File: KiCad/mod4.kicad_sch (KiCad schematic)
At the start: 46 parts, among them M7 Fan_4pin, M8 Fan_4pin

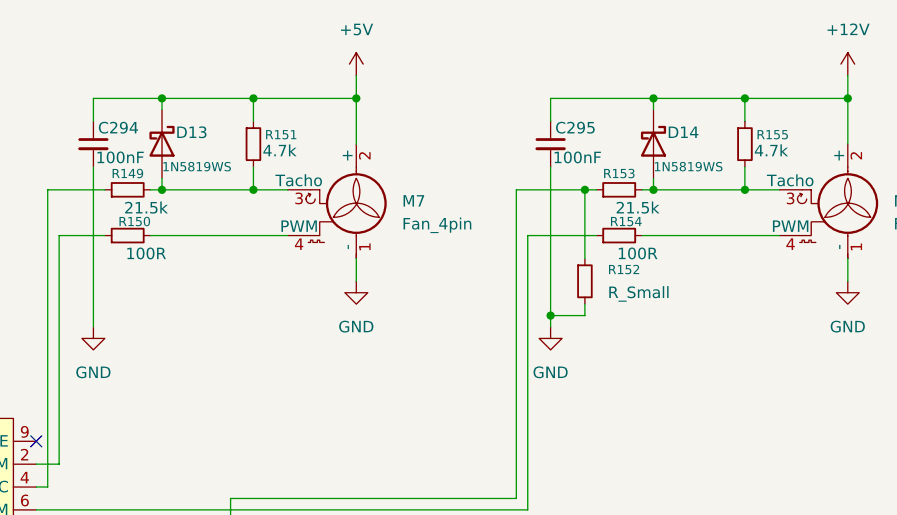
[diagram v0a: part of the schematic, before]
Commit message: Fix some diodes and resistors
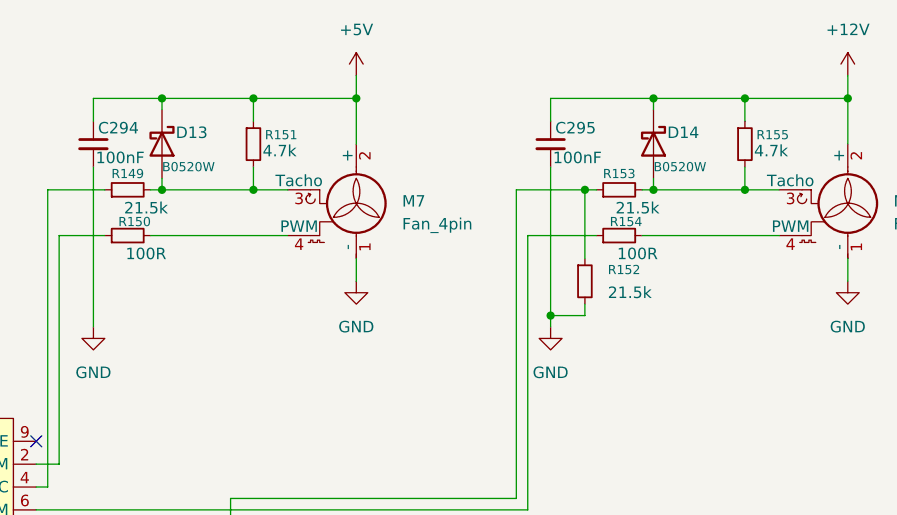
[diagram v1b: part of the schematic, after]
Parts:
- D13, D14: value 1N5819WS -> B0520W
- R152: value R_Small -> 21.5k
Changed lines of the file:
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@@
 			)
 		)
-		(property "Value" "R_Small"
+		(property "Value" "21.5k"
 			(at 391.16 68.5799 0)
 			(effects
@@
 			)
 		)
-		(property "Value" "1N5819WS"
+		(property "Value" "B0520W"
 			(at 396.24 54.61 90)
 			(effects
@@
 			)
 		)
-		(property "Value" "1N5819WS"
+		(property "Value" "B0520W"
 			(at 341.63 54.61 90)
 			(effects

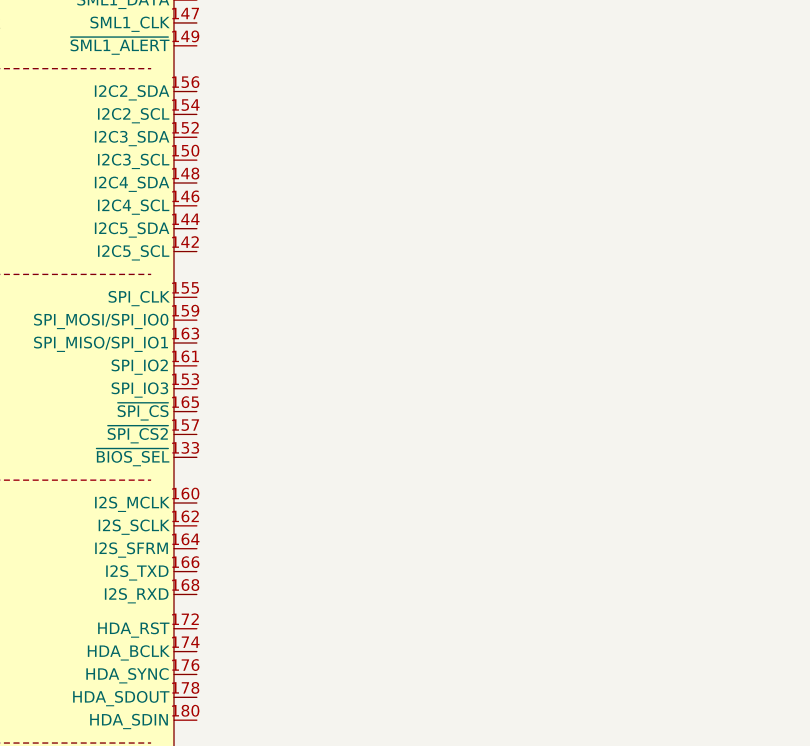
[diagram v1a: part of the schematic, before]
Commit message: Add external BIOS flash
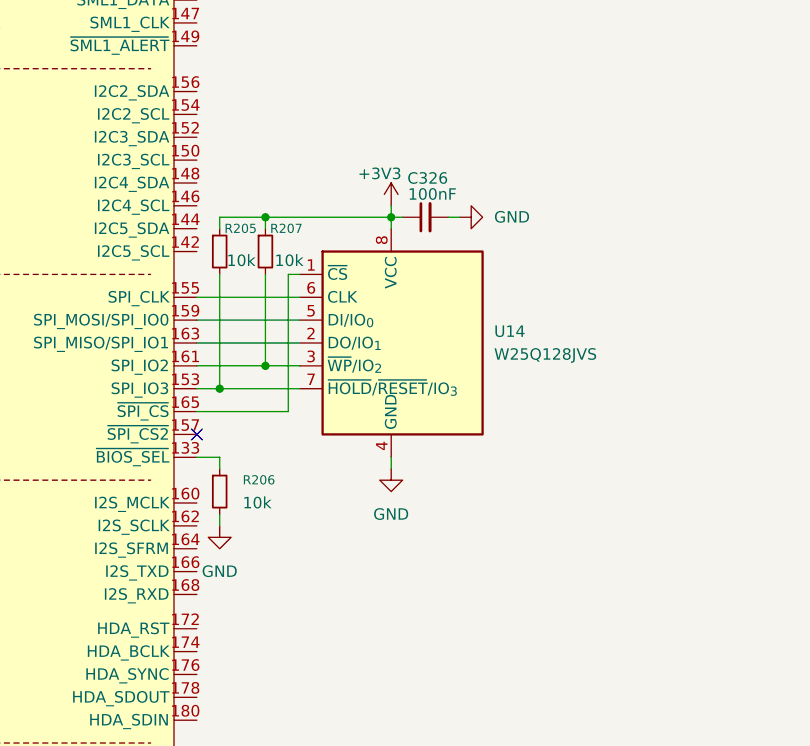
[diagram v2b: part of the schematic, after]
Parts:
- added C326: 100nF, symbol Device:C_Small
- added R205, R206, R207: 10k, symbol Device:R_Small
- added U14: W25Q128JVS, Package_SO:SOIC-8_5.3x5.3mm_P1.27mm, symbol Memory_Flash:W25Q128JVS
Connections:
- net +3V3: now also C326.1, R205.1, R207.1, U14.8 (VCC)
- net GND: now also C326.2, R206.2, U14.4 (GND)
- net at A4.133 (~{BIOS_SEL}): now also R206.1
- net at A4.153 (SPI_IO3): now also R205.2, U14.7 (~{HOLD}/~{RESET}/IO_{3})
- net at A4.155 (SPI_CLK): now also U14.6 (CLK)
- net at A4.159 (SPI_MOSI/SPI_IO0): now also U14.5 (DI/IO_{0})
- net at A4.161 (SPI_IO2): now also R207.2, U14.3 (~{WP}/IO_{2})
- net at A4.163 (SPI_MISO/SPI_IO1): now also U14.2 (DO/IO_{1})
- net at A4.165 (~{SPI_CS}): now also U14.1 (~{CS})
- no-connect marks 1 -> 2

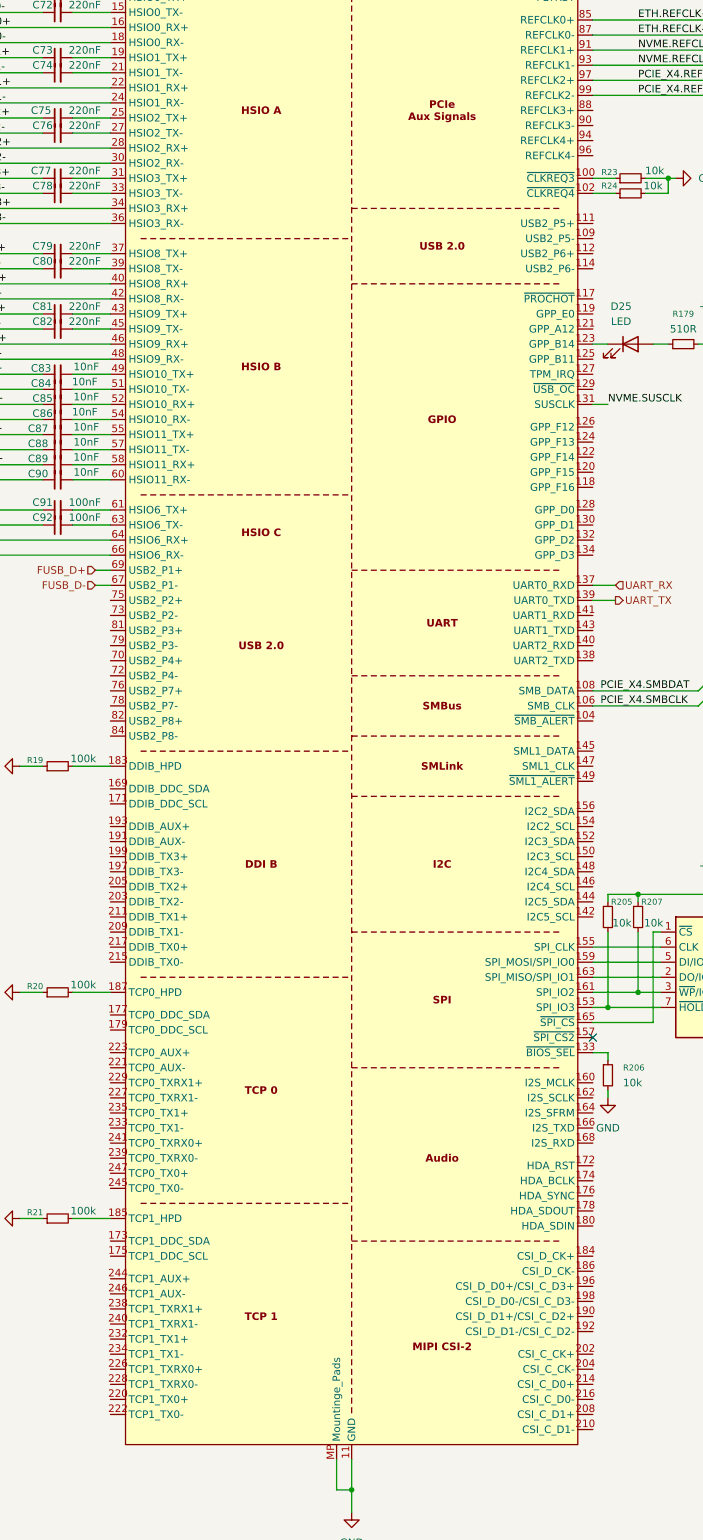
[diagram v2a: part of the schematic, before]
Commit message: Remove 0.95V Power Supply, Replace 3.3V Standby Power Supply
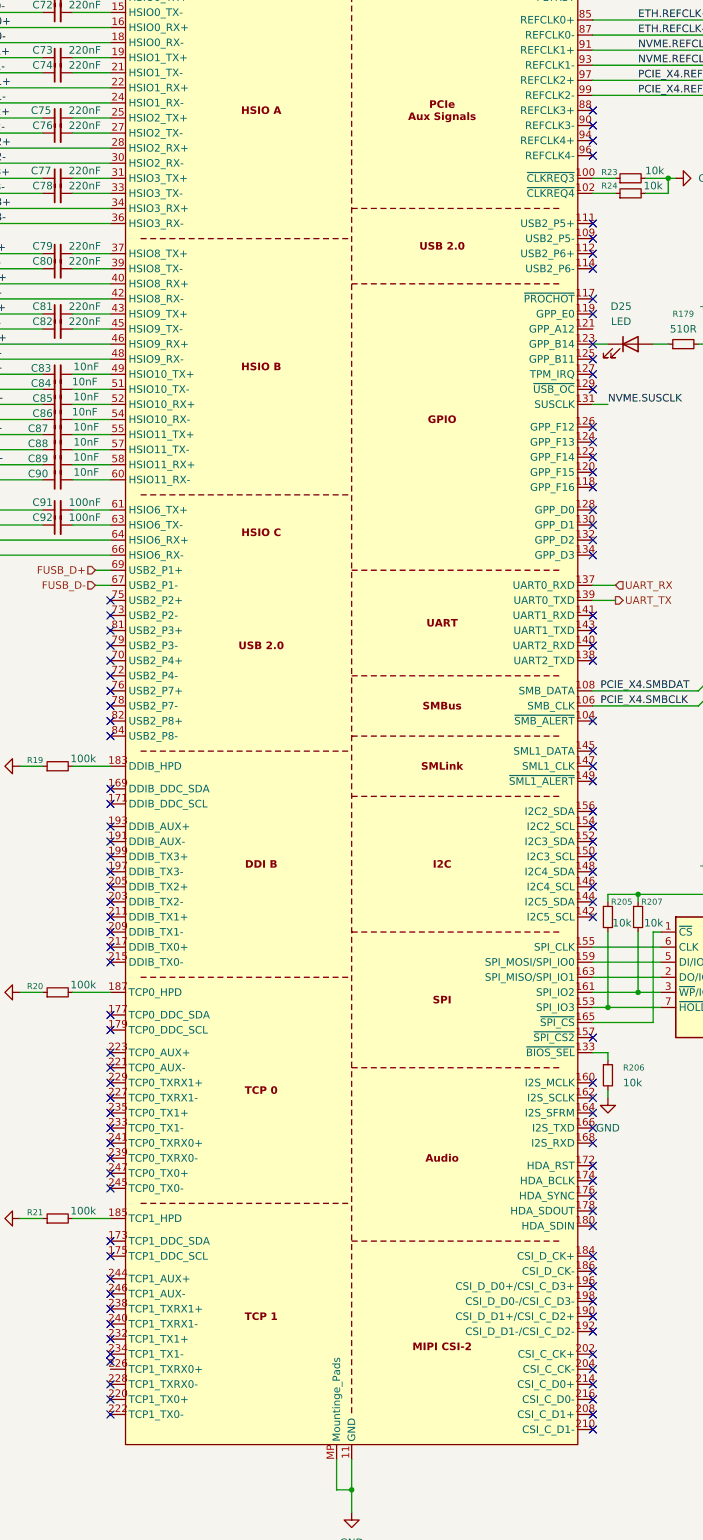
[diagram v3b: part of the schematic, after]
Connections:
- no-connect marks 2 -> 109

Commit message: Work though ERC errors
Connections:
- net PCIE_X4.SMBCLK renamed ETH.SMBCLK
- net PCIE_X4.SMBDAT renamed ETH.SMBDAT
- no-connect marks 109 -> 112
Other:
- moved on the sheet: R22

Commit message: Re-annotate components
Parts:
- C100: renamed from C91; value 100nF -> 220nF
- C101: renamed from C92; value 100nF -> 220nF
- renumbered C294 to C102, C326 to C103, C295 to C104, C71 to C80, C72 to C81, C73 to C82, C74 to C83, C75 to C84, C76 to C85, C77 to C86, C78 to C87, C79 to C88, C80 to C89, C81 to C90, C82 to C91, C83 to C92, C84 to C93, C85 to C94, C86 to C95, C87 to C96, C88 to C97, C89 to C98, C90 to C99, D20 to D13, D25 to D14, D13 to D15, D14 to D16, R166 to R63, R19 to R64, R20 to R65, R21 to R66, R22 to R67, R205 to R68, R206 to R69, R23 to R70, R24 to R71, R207 to R72, R149 to R73, R150 to R74, R179 to R75, R151 to R76, R152 to R77, R153 to R78, R154 to R79, R155 to R80, U14 to U4

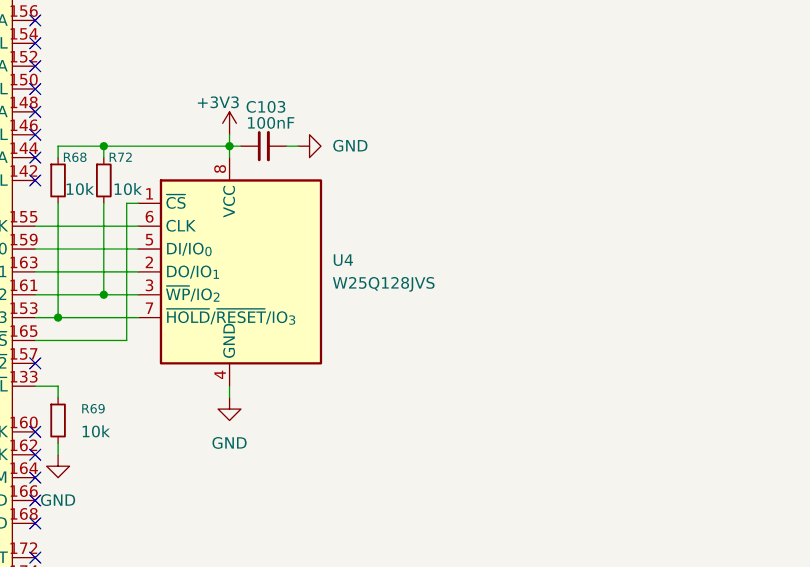
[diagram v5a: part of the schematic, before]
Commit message: Add TVS diodes for ESD protection
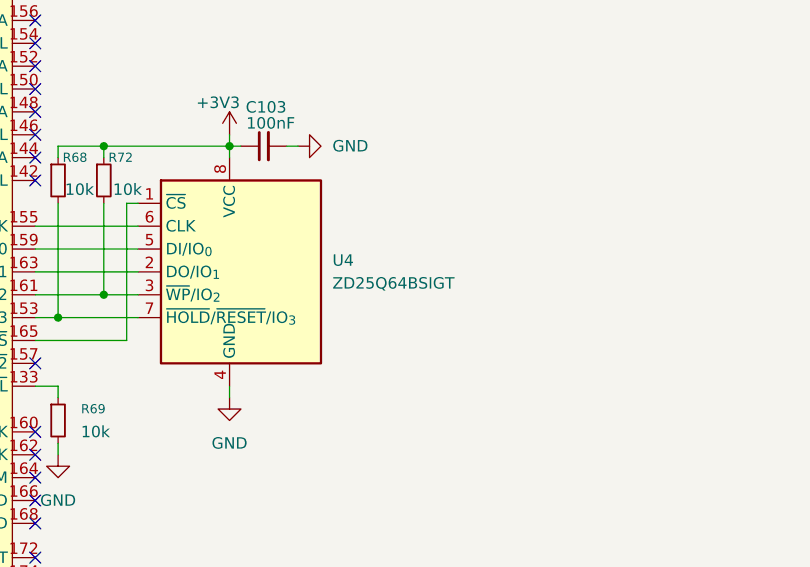
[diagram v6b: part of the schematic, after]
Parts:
- U4: value W25Q128JVS -> ZD25Q64BSIGT
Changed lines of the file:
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@@
 			)
 		)
-		(property "Value" "W25Q128JVS"
+		(property "Value" "ZD25Q64BSIGT"
 			(at 360.68 269.2399 0)
 			(effects

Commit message: Add more footprints
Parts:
- A4: footprint Module_LattePanda:LattePanda_Module_H8.0mm_Horizontal -> 124B-150A02:ATTEND_124B-150A02
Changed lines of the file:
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@@
 			)
 		)
-		(property "Footprint" "Module_LattePanda:LattePanda_Module_H8.0mm_Horizontal"
+		(property "Footprint" "124B-150A02:ATTEND_124B-150A02"
 			(at 287.02 204.47 0)
 			(effects

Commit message: Add more footprints
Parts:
- C100, C101, C102, C103, C104, C80, C81, C82, C83, C84, C85, C86, C87, C88, C89, C90, C91, C92, C93, C94, C95, C96, C97, C98, C99: footprint (none) -> Capacitor_SMD:C_0603_1608Metric
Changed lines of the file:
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@@
 			)
 		)
-		(property "Footprint" ""
+		(property "Footprint" "Capacitor_SMD:C_0603_1608Metric"
 			(at 237.49 176.53 0)
 			(effects
@@
 			)
 		)
-		(property "Footprint" ""
+		(property "Footprint" "Capacitor_SMD:C_0603_1608Metric"
 			(at 237.49 181.61 0)
 			(effects
@@
 			)
 		)
-		(property "Footprint" ""
+		(property "Footprint" "Capacitor_SMD:C_0603_1608Metric"
 			(at 237.49 123.19 0)
 			(effects
@@
 			)
 		)
-		(property "Footprint" ""
+		(property "Footprint" "Capacitor_SMD:C_0603_1608Metric"
 			(at 237.49 115.57 0)
 			(effects
@@
 			)
 		)
-		(property "Footprint" ""
+		(property "Footprint" "Capacitor_SMD:C_0603_1608Metric"
 			(at 384.81 52.07 0)
 			(effects
@@
 			)
 		)
-		(property "Footprint" ""
+		(property "Footprint" "Capacitor_SMD:C_0603_1608Metric"
 			(at 237.49 168.91 0)
 			(effects
@@
 			)
 		)
-		(property "Footprint" ""
+		(property "Footprint" "Capacitor_SMD:C_0603_1608Metric"
 			(at 237.49 166.37 0)
 			(effects
@@
 			)
 		)
-		(property "Footprint" ""
+		(property "Footprint" "Capacitor_SMD:C_0603_1608Metric"
 			(at 237.49 191.77 0)
 			(effects
@@
 			)
 		)
-		(property "Footprint" ""
+		(property "Footprint" "Capacitor_SMD:C_0603_1608Metric"
 			(at 237.49 184.15 0)
 			(effects
@@
 			)
 		)
-		(property "Footprint" ""
+		(property "Footprint" "Capacitor_SMD:C_0603_1608Metric"
 			(at 237.49 102.87 0)
 			(effects
@@
 			)
 		)
-		(property "Footprint" ""
+		(property "Footprint" "Capacitor_SMD:C_0603_1608Metric"
 			(at 237.49 173.99 0)
 			(effects
@@
 			)
 		)
-		(property "Footprint" ""
+		(property "Footprint" "Capacitor_SMD:C_0603_1608Metric"
 			(at 237.49 105.41 0)
 			(effects
@@
 			)
 		)
-		(property "Footprint" ""
+		(property "Footprint" "Capacitor_SMD:C_0603_1608Metric"
 			(at 237.49 171.45 0)
 			(effects
@@
 			)
 		)
-		(property "Footprint" ""
+		(property "Footprint" "Capacitor_SMD:C_0603_1608Metric"
 			(at 237.49 113.03 0)
 			(effects
@@
 			)
 		)
-		(property "Footprint" ""
+		(property "Footprint" "Capacitor_SMD:C_0603_1608Metric"
 			(at 237.49 158.75 0)
 			(effects
@@
 			)
 		)
-		(property "Footprint" ""
+		(property "Footprint" "Capacitor_SMD:C_0603_1608Metric"
 			(at 237.49 179.07 0)
 			(effects
@@
 			)
 		)
-		(property "Footprint" ""
+		(property "Footprint" "Capacitor_SMD:C_0603_1608Metric"
 			(at 237.49 189.23 0)
 			(effects
@@
 			)
 		)
-		(property "Footprint" ""
+		(property "Footprint" "Capacitor_SMD:C_0603_1608Metric"
 			(at 237.49 156.21 0)
 			(effects
@@
 			)
 		)
-		(property "Footprint" ""
+		(property "Footprint" "Capacitor_SMD:C_0603_1608Metric"
 			(at 334.01 52.07 0)
 			(effects
@@
 			)
 		)
-		(property "Footprint" ""
+		(property "Footprint" "Capacitor_SMD:C_0603_1608Metric"
 			(at 353.06 254 0)
 			(effects
@@
 			)
 		)
-		(property "Footprint" ""
+		(property "Footprint" "Capacitor_SMD:C_0603_1608Metric"
 			(at 237.49 125.73 0)
 			(effects
@@
 			)
 		)
-		(property "Footprint" ""
+		(property "Footprint" "Capacitor_SMD:C_0603_1608Metric"
 			(at 237.49 148.59 0)
 			(effects
@@
 			)
 		)
-		(property "Footprint" ""
+		(property "Footprint" "Capacitor_SMD:C_0603_1608Metric"
 			(at 237.49 133.35 0)
 			(effects
@@
 			)
 		)
-		(property "Footprint" ""
+		(property "Footprint" "Capacitor_SMD:C_0603_1608Metric"
 			(at 237.49 135.89 0)
 			(effects
@@
 			)
 		)
-		(property "Footprint" ""
+		(property "Footprint" "Capacitor_SMD:C_0603_1608Metric"
 			(at 237.49 146.05 0)
 			(effects
